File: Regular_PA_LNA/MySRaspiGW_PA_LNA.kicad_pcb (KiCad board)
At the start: 2 copper layers, 11.5 x 11.9 mm, 5 parts, among them P1 CONN_02X04, U1 NRF24L01

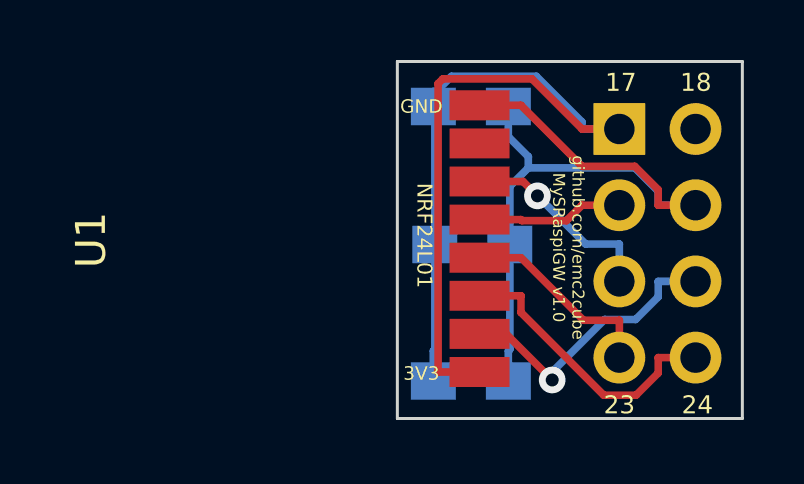
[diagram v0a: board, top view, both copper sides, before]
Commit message: v1.1 IRQ support
Added IRQ support on pin 18
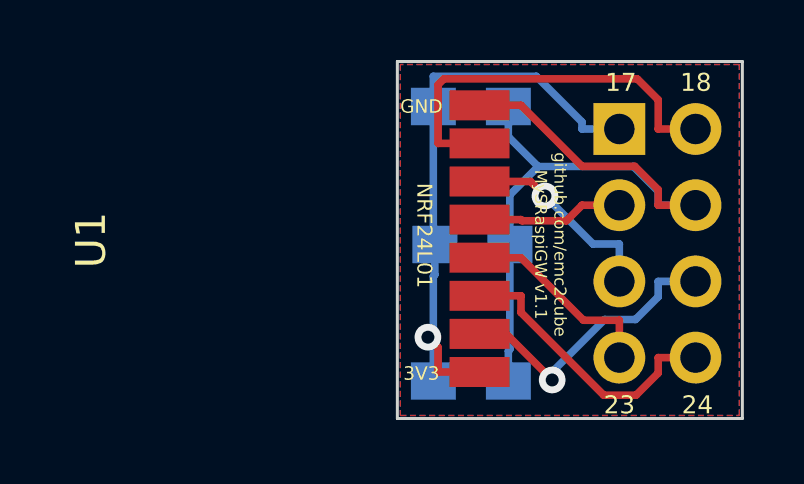
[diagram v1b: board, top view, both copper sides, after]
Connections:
- P1 pad 2: Net-(P1-Pad2) -> IRQ
- U1 pad 8: Net-(U1-Pad8) -> IRQ
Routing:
- net +3V3: track 35.2 -> 20.6 mm, vias 0 -> 1
- net IRQ: track 0.00 -> 13.3 mm
- added copper zone on B.Cu, net GND
- added copper zone on F.Cu, net GND
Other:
- board text added: "github.com/emc2cube MySRaspiGW v1.1"
- board text removed: "github.com/emc2cube MySRaspiGW v1.0"
